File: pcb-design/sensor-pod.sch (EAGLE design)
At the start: 14 parts, among them X1 PH_SENSOR, X10 I2C_3, X11 3.3V, X12 3.3V, X15 MB-LEFT, X16 MB-RIGHT, X2 5V, X3 TURBIDITY, X4 5V, X5 TEMPERATURE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

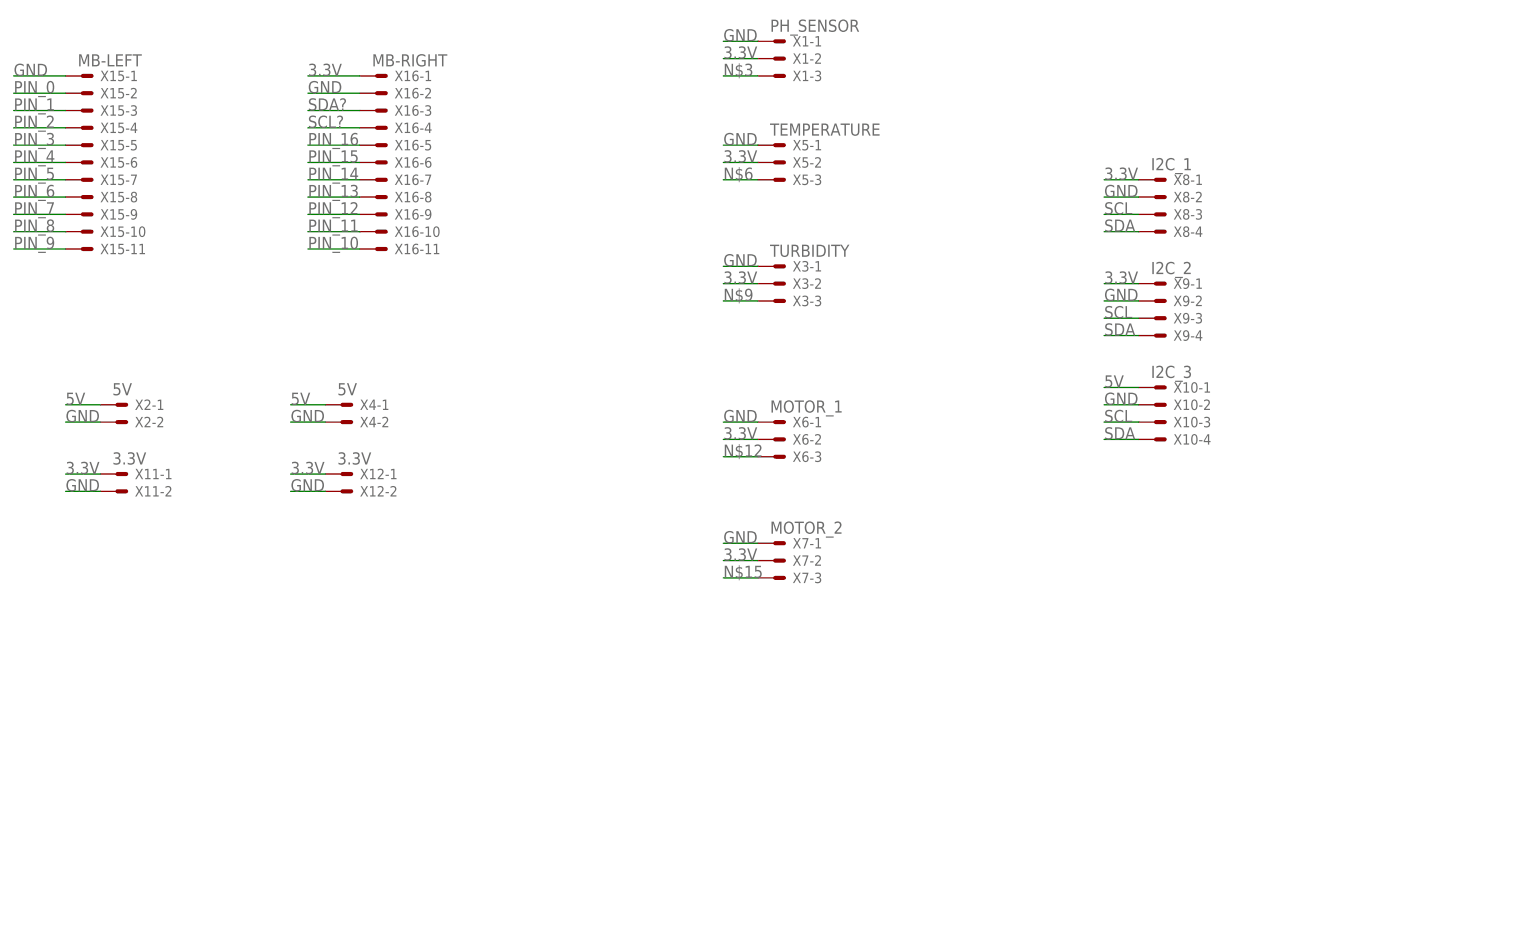
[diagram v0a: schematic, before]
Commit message: pcb-design: Changed board layout and assigned pins for sensors.
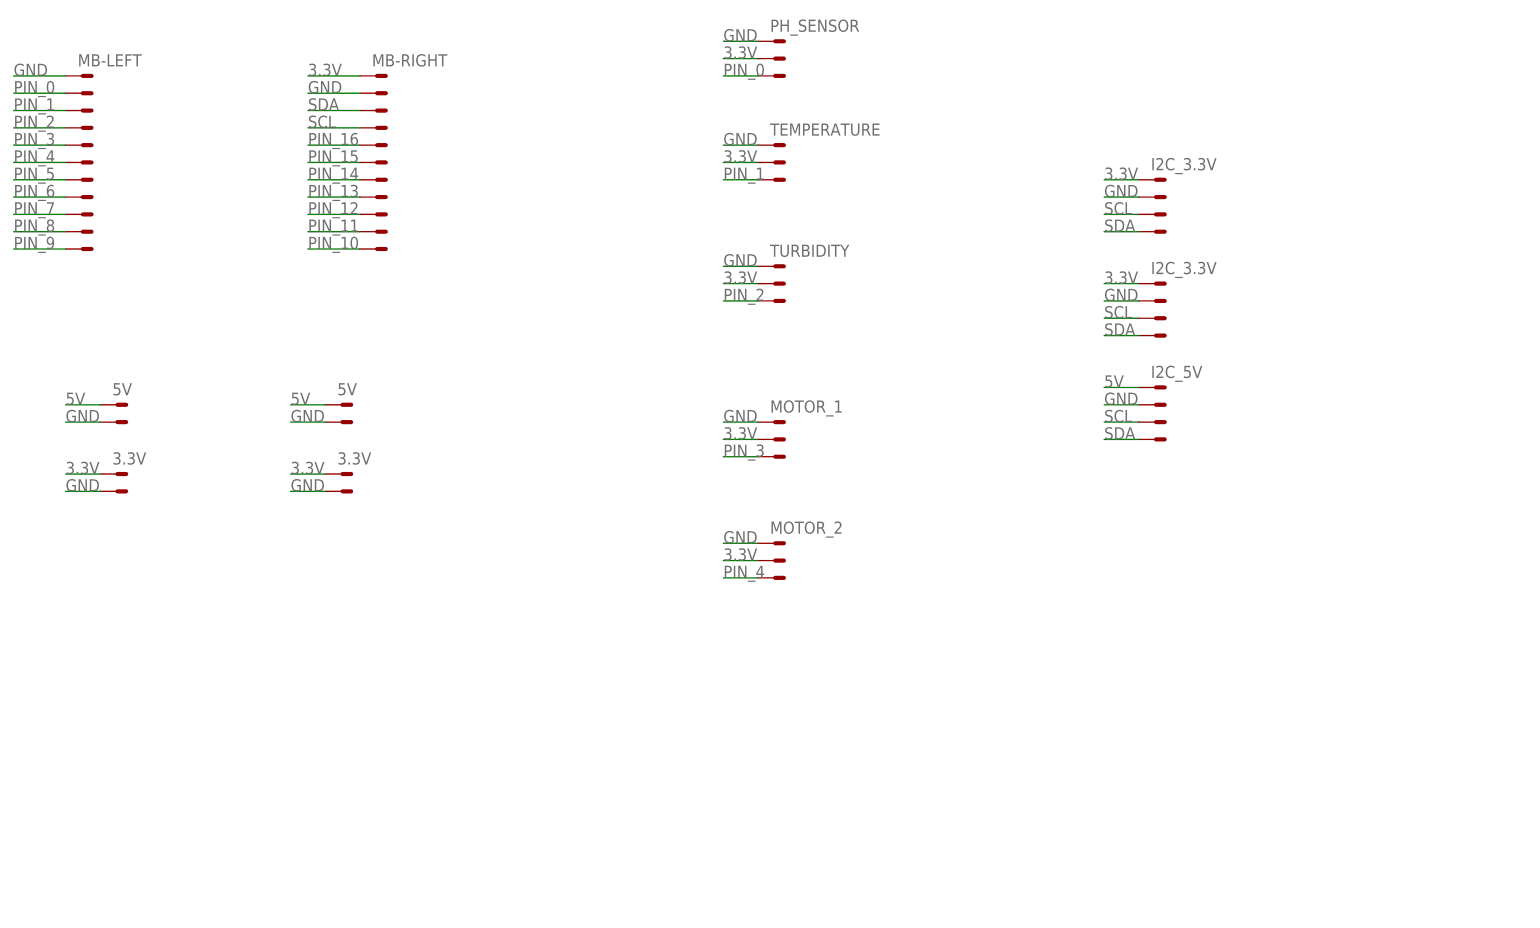
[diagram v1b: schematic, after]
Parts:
- X10: value I2C_3 -> I2C_5V
- X8: value I2C_1 -> I2C_3.3V
- X9: value I2C_2 -> I2C_3.3V
- renumbered X2 to 1
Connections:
- removed net N$12: X6-3.S
- removed net N$15: X7-3.S
- removed net N$3: X1-3.S
- removed net N$6: X5-3.S
- removed net N$9: X3-3.S
- removed net SCL?: X16-4.S
- removed net SDA?: X16-3.S
- net PIN_0: now also X1-3.S
- net PIN_1: now also X5-3.S
- net PIN_2: now also X3-3.S
- net PIN_3: now also X6-3.S
- net PIN_4: now also X7-3.S
- net SCL: now also X16-4.S
- net SDA: now also X16-3.S

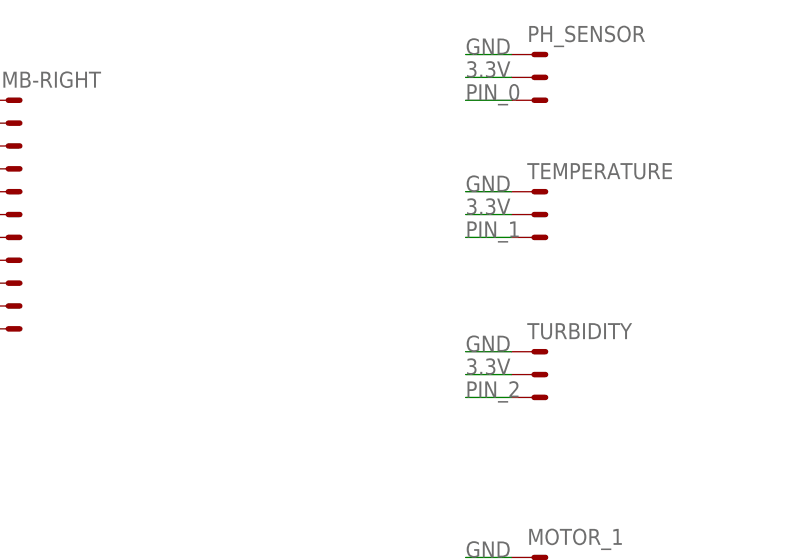
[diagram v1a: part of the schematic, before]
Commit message: Sensor pod: Fix temp sensor code to use P8 + Changed PCB to match
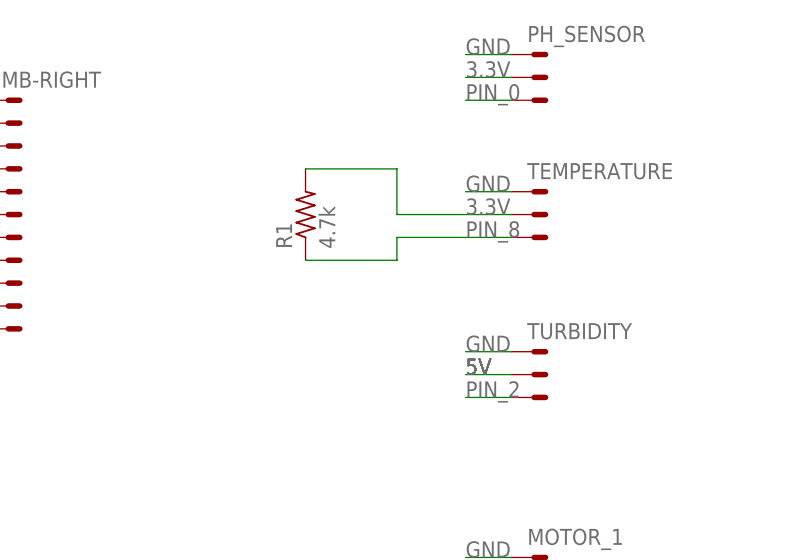
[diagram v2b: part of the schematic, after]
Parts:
- added R1: 4.7k, rcl:R-US_0204/7
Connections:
- net 3.3V: now also R1.2; no longer X3-2.S
- net 5V: now also X3-2.S
- net PIN_1: no longer X5-3.S
- net PIN_8: now also R1.1, X5-3.S
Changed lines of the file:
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@@
 <part name="X15" library="con-molex" library_urn="urn:adsk.eagle:library:165" deviceset="22-23-2111" device="" package3d_urn="urn:adsk.eagle:package:8078642/1" value="MB-LEFT"/>
 <part name="X16" library="con-molex" library_urn="urn:adsk.eagle:library:165" deviceset="22-23-2111" device="" package3d_urn="urn:adsk.eagle:package:8078642/1" value="MB-RIGHT"/>
+<part name="R1" library="rcl" library_urn="urn:adsk.eagle:library:334" deviceset="R-US_" device="0204/7" package3d_urn="urn:adsk.eagle:package:23498/2" value="4.7k"/>
 </parts>
 <sheets>
@@
 <instance part="X16" gate="-10" x="63.5" y="33.02" smashed="yes"/>
 <instance part="X16" gate="-11" x="63.5" y="30.48" smashed="yes"/>
+<instance part="R1" gate="G$1" x="96.52" y="43.18" smashed="yes" rot="R90">
+<attribute name="NAME" x="95.0214" y="39.37" size="1.778" layer="95" rot="R90"/>
+<attribute name="VALUE" x="99.822" y="39.37" size="1.778" layer="96" rot="R90"/>
+</instance>
 </instances>
 <busses>
@@
 <label x="170.18" y="10.16" size="1.778" layer="95"/>
 </segment>
+<segment>
+<pinref part="X3" gate="-2" pin="S"/>
+<wire x1="119.38" y1="25.4" x2="114.3" y2="25.4" width="0.1524" layer="91"/>
+<label x="114.3" y="25.4" size="1.778" layer="95"/>
+<label x="114.3" y="25.4" size="1.778" layer="95"/>
+<label x="114.3" y="25.4" size="1.778" layer="95"/>
+</segment>
 </net>
 <net name="GND" class="0">
@@
 <segment>
 <pinref part="X5" gate="-2" pin="S"/>
-<wire x1="119.38" y1="43.18" x2="114.3" y2="43.18" width="0.1524" layer="91"/>
 <label x="114.3" y="43.18" size="1.778" layer="95"/>
-</segment>
-<segment>
-<pinref part="X3" gate="-2" pin="S"/>
-<wire x1="119.38" y1="25.4" x2="114.3" y2="25.4" width="0.1524" layer="91"/>
-<label x="114.3" y="25.4" size="1.778" layer="95"/>
+<wire x1="119.38" y1="43.18" x2="106.68" y2="43.18" width="0.1524" layer="91"/>
+<wire x1="106.68" y1="43.18" x2="106.68" y2="48.26" width="0.1524" layer="91"/>
+<pinref part="R1" gate="G$1" pin="2"/>
+<wire x1="106.68" y1="48.26" x2="96.52" y2="48.26" width="0.1524" layer="91"/>
 </segment>
 <segment>
@@
 <label x="10.16" y="50.8" size="1.778" layer="95"/>
 </segment>
-<segment>
-<pinref part="X5" gate="-3" pin="S"/>
-<wire x1="119.38" y1="40.64" x2="114.3" y2="40.64" width="0.1524" layer="91"/>
-<label x="114.3" y="40.64" size="1.778" layer="95"/>
-</segment>
 </net>
 <net name="PIN_2" class="0">
@@
 <wire x1="17.78" y1="33.02" x2="10.16" y2="33.02" width="0.1524" layer="91"/>
 <label x="10.16" y="33.02" size="1.778" layer="95"/>
+</segment>
+<segment>
+<pinref part="X5" gate="-3" pin="S"/>
+<label x="114.3" y="40.64" size="1.778" layer="95"/>
+<wire x1="119.38" y1="40.64" x2="106.68" y2="40.64" width="0.1524" layer="91"/>
+<wire x1="106.68" y1="40.64" x2="106.68" y2="38.1" width="0.1524" layer="91"/>
+<pinref part="R1" gate="G$1" pin="1"/>
+<wire x1="106.68" y1="38.1" x2="96.52" y2="38.1" width="0.1524" layer="91"/>
 </segment>
 </net>
@@
 packages will not be understood (or retained) with this version.
 </note>
+<note version="8.4" severity="warning">
+Since Version 8.4, EAGLE supports properties for SPICE simulation.
+Probes in schematics and SPICE mapping objects found in parts and library devices
+will not be understood with this version. Update EAGLE to the latest version
+for full support of SPICE simulation.
+</note>
 </compatibility>

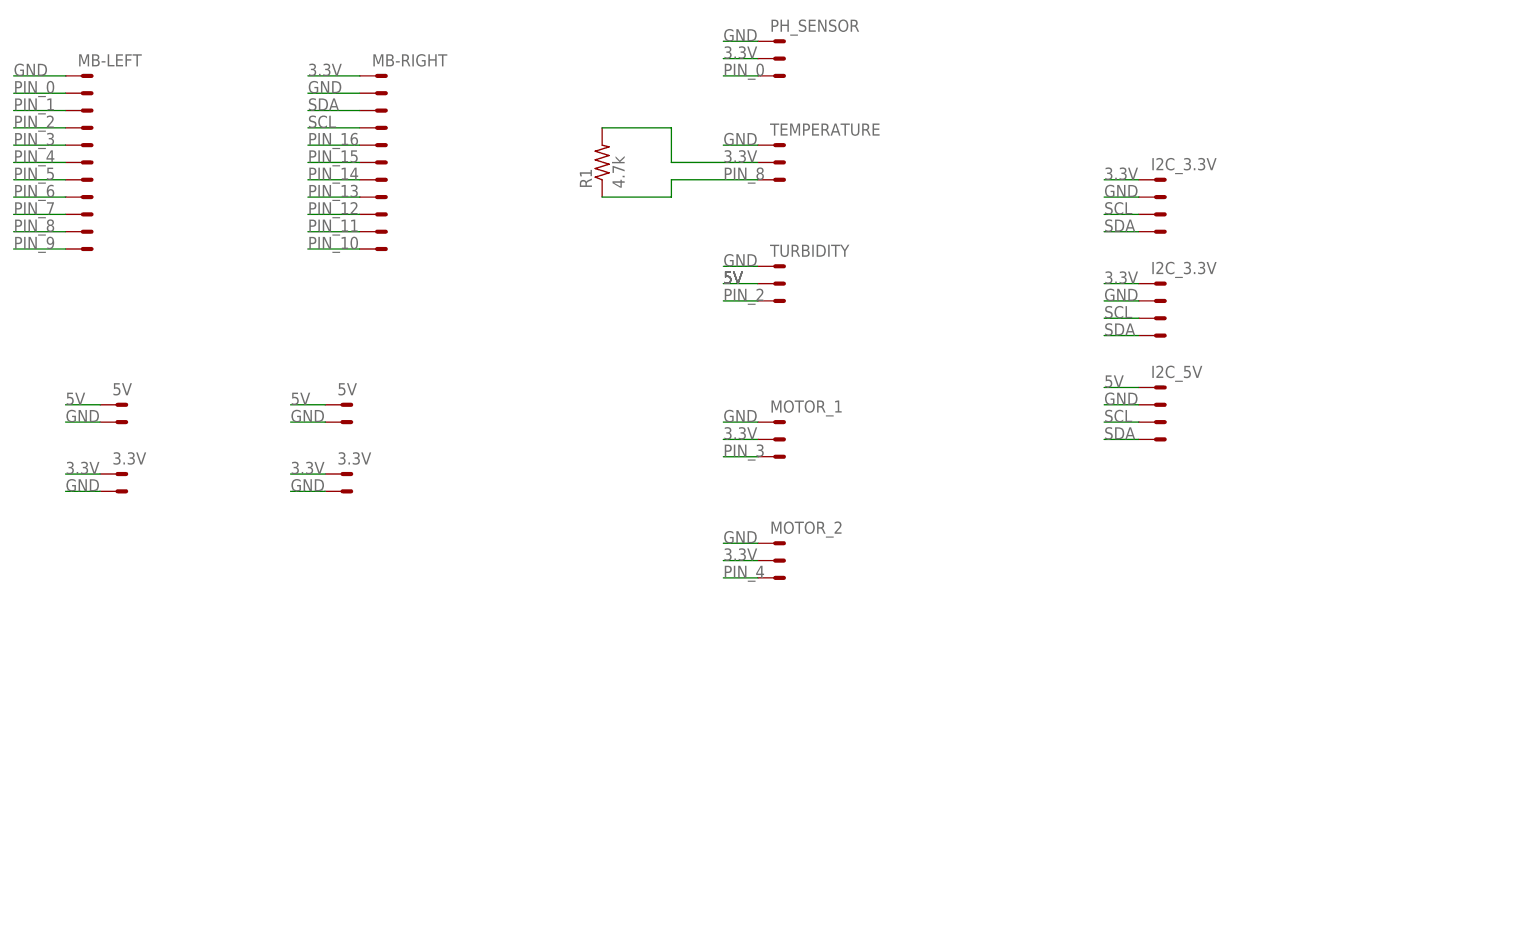
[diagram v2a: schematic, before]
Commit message: pcb-design: Draft 2 Added LDR and power LED's + Changed board size/placement
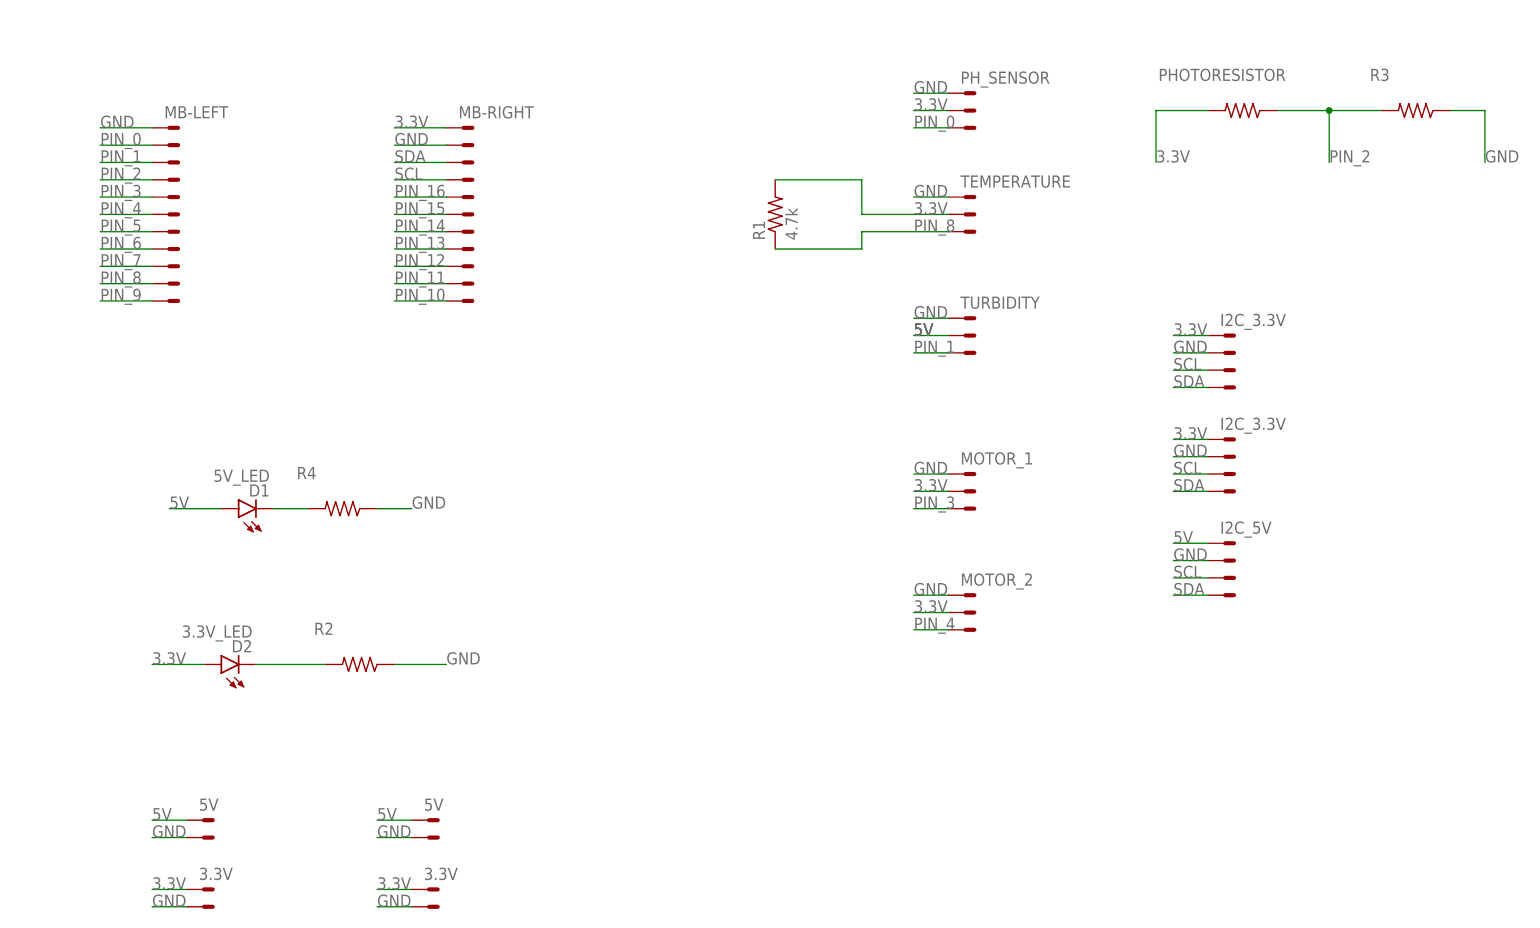
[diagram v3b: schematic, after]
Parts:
- added D1: 5V_LED, led:SFH482
- added D2: 3.3V_LED, led:SFH482
- added PHOTORESISTOR, R2, R3, R4: (no value), rcl:R-US_0204/7
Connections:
- new net N$1: D1.C, R4.2
- new net N$2: D2.C, R2.2
- net 3.3V: now also D2.A, PHOTORESISTOR.2
- net 5V: now also D1.A
- net GND: now also R2.1, R3.1, R4.1
- net PIN_1: now also X3-3.S
- net PIN_2: now also PHOTORESISTOR.1, R3.2; no longer X3-3.S
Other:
- moved on the sheet: R1
